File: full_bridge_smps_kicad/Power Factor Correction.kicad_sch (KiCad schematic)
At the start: 44 parts, among them Q2 MMBT2904, Q5 IPA60R280C6, Q6 IPA60R280C6, Q6 SI2309, Q7 IPW60R041C6, T1 PA1005.100NL, T2 PA1005.100NL, U4 TL431ACDBZR, U5 UCC27324D, U6 UCC27324D

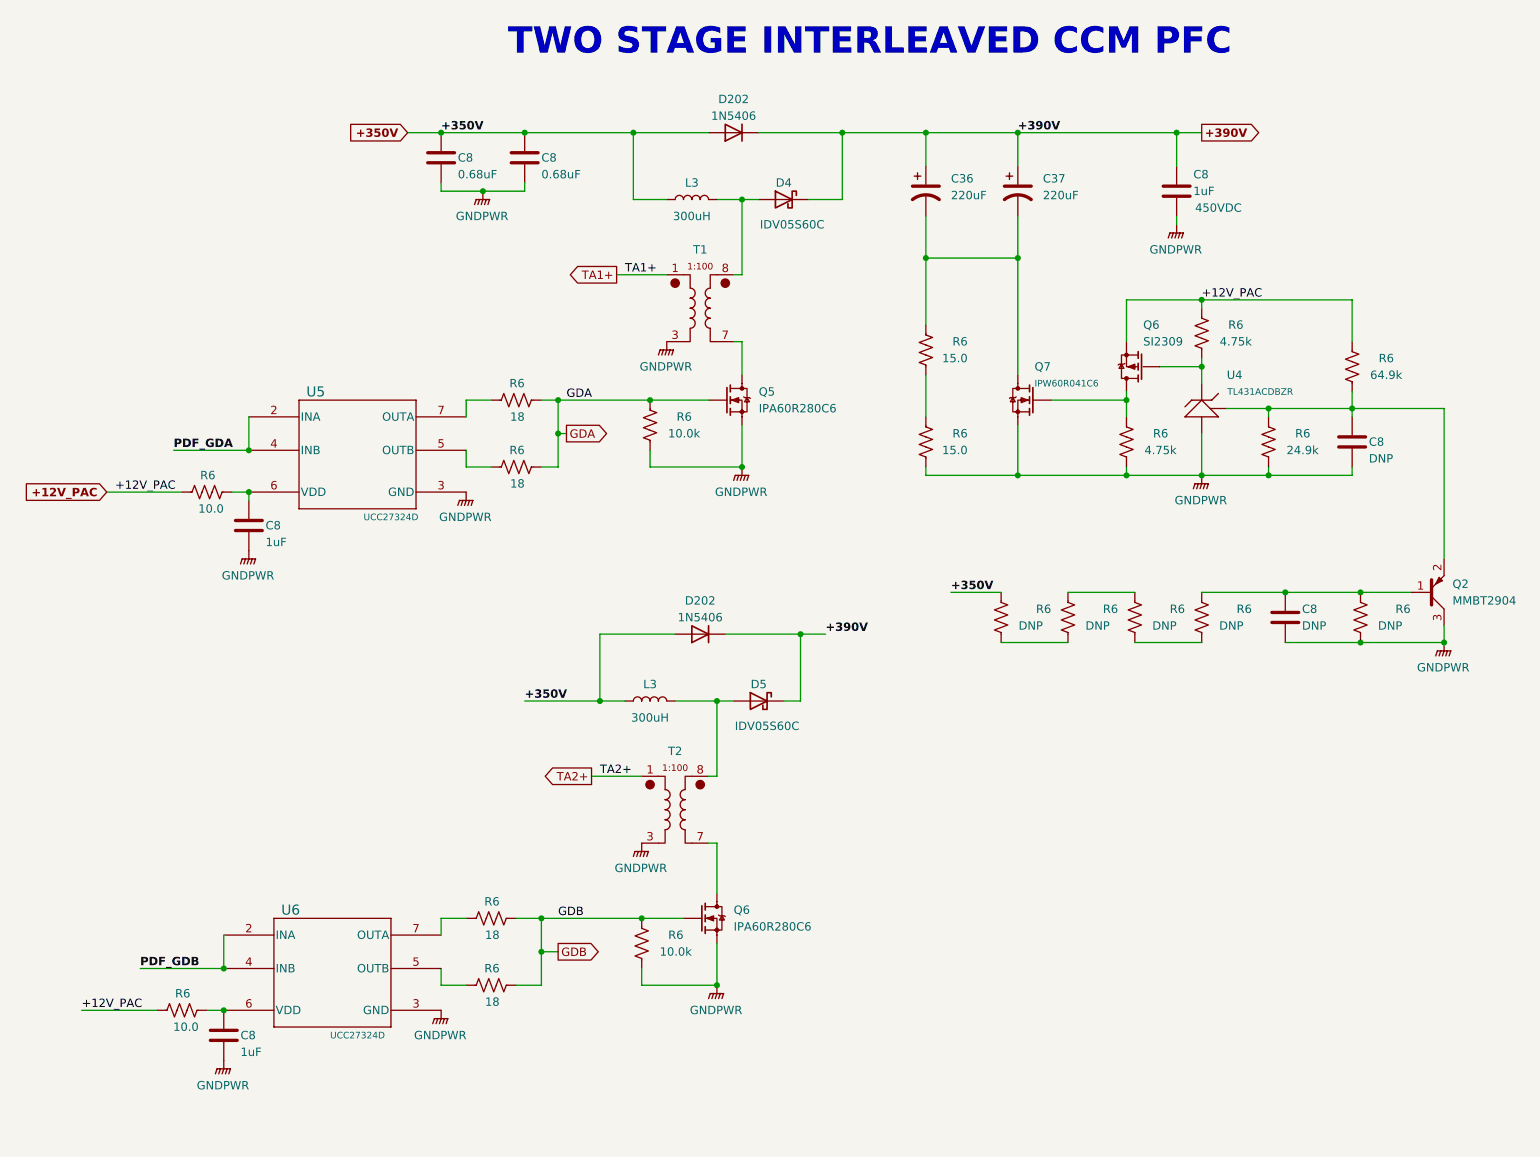
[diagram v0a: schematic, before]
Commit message: Finishing power factor correction sheets, moving to power conversion
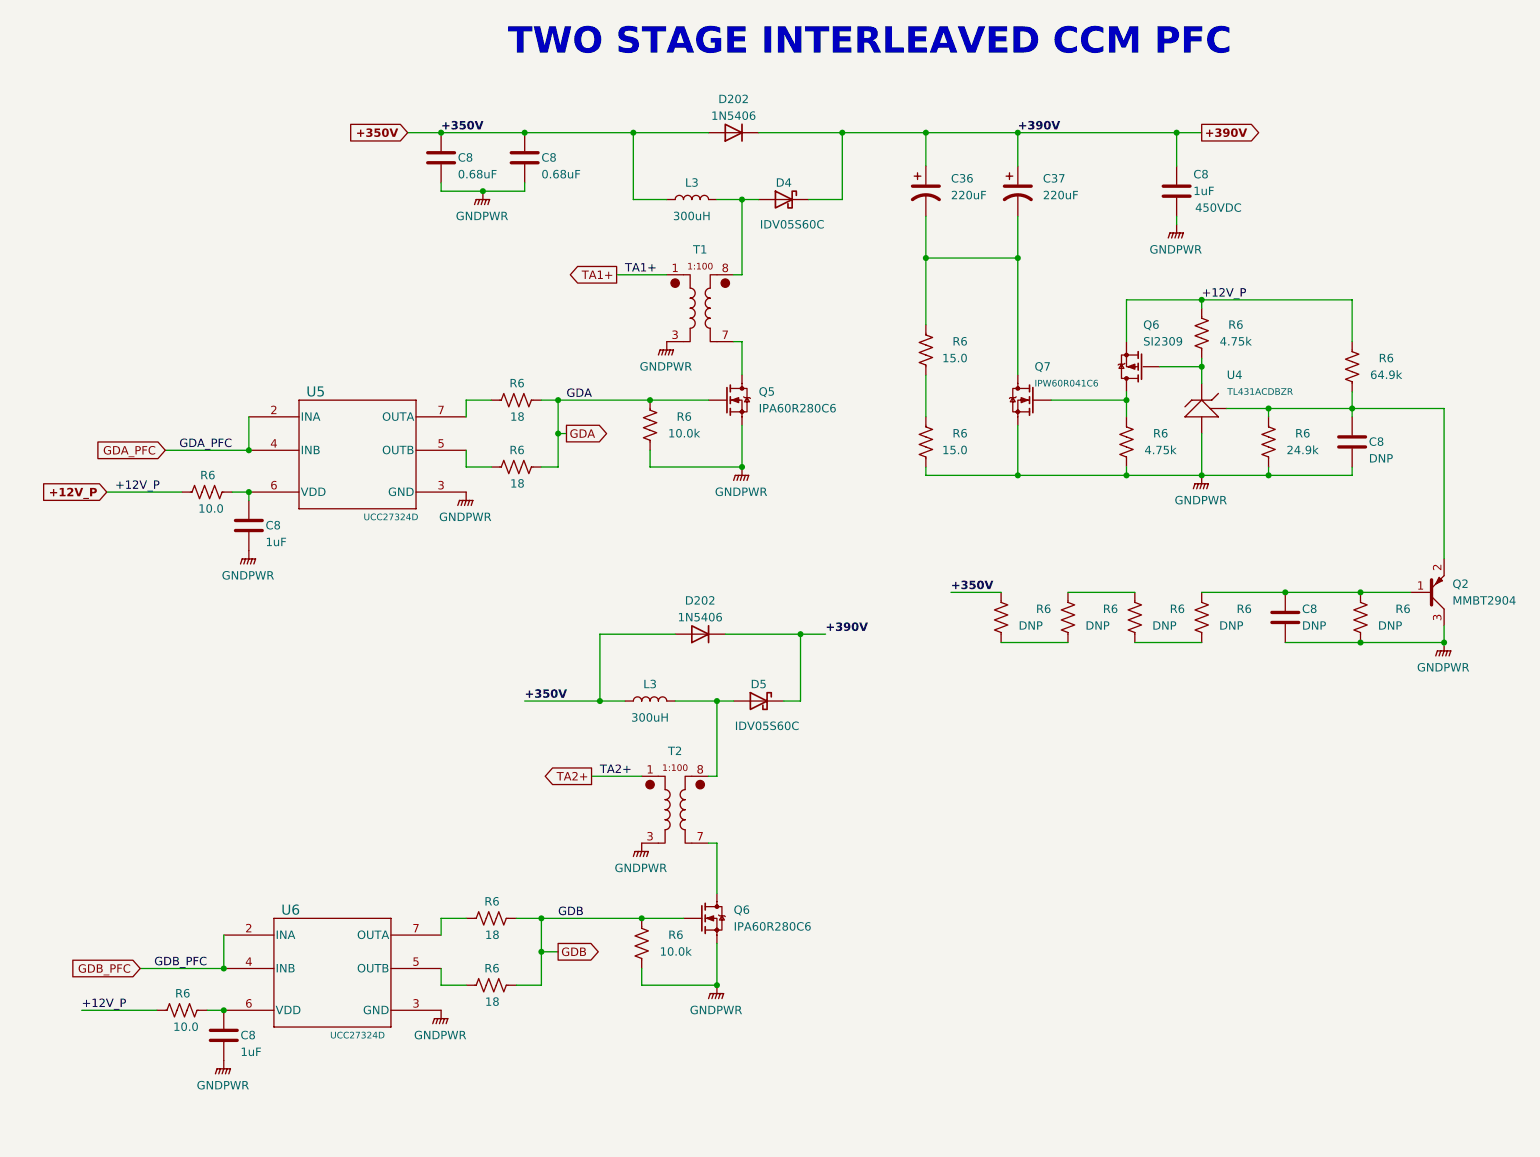
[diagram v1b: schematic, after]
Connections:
- net +12V_PAC renamed +12V_P
- net PDF_GDA renamed GDA_PFC
- net PDF_GDB renamed GDB_PFC
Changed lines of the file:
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@@
     (stroke (width 0) (type default))
   )
-  (wire (pts (xy 41.91 92.71) (xy 53.34 92.71))
+  (wire (pts (xy 40.64 92.71) (xy 53.34 92.71))
     (stroke (width 0) (type default))
   )
@@
     (effects (font (size 1.27 1.27)) (justify left bottom))
   )
-  (label "+12V_PAC" (at 27.94 177.8 0) (fields_autoplaced)
+  (label "+12V_P" (at 27.94 177.8 0) (fields_autoplaced)
     (effects (font (size 1.27 1.27)) (justify left bottom))
   )
-  (label "+12V_PAC" (at 33.02 99.06 0) (fields_autoplaced)
+  (label "+12V_P" (at 33.02 99.06 0) (fields_autoplaced)
     (effects (font (size 1.27 1.27)) (justify left bottom))
   )
@@
     (effects (font (size 1.27 1.27)) (justify left bottom))
   )
+  (label "GDA_PFC" (at 50.8 92.71 180) (fields_autoplaced)
+    (effects (font (size 1.27 1.27)) (justify right bottom))
+  )
   (label "+390V" (at 170.18 44.45 0) (fields_autoplaced)
     (effects (font (size 1.27 1.27) bold) (justify left bottom))
+  )
+  (label "GDB_PFC" (at 46.99 171.45 180) (fields_autoplaced)
+    (effects (font (size 1.27 1.27)) (justify right bottom))
   )
   (label "+350V" (at 95.25 130.81 0) (fields_autoplaced)
@@
     (effects (font (size 1.27 1.27) bold) (justify left bottom))
   )
-  (label "PDF_GDB" (at 36.83 171.45 0) (fields_autoplaced)
-    (effects (font (size 1.27 1.27) bold) (justify left bottom))
-  )
   (label "+390V" (at 140.97 120.65 0) (fields_autoplaced)
     (effects (font (size 1.27 1.27) bold) (justify left bottom))
@@
     (effects (font (size 1.27 1.27) bold) (justify left bottom))
   )
-  (label "+12V_PAC" (at 198.12 69.85 0) (fields_autoplaced)
+  (label "+12V_P" (at 198.12 69.85 0) (fields_autoplaced)
     (effects (font (size 1.27 1.27)) (justify left bottom))
   )
   (label "TA2+" (at 106.68 142.24 0) (fields_autoplaced)
     (effects (font (size 1.27 1.27)) (justify left bottom))
-  )
-  (label "PDF_GDA" (at 41.91 92.71 0) (fields_autoplaced)
-    (effects (font (size 1.27 1.27) bold) (justify left bottom))
   )
   (global_label "GDB" (shape output) (at 100.33 168.91 0) (fields_autoplaced)
@@
     )
   )
-  (global_label "+12V_PAC" (shape input) (at 31.75 99.06 180) (fields_autoplaced)
-    (effects (font (size 1.27 1.27) bold) (justify right))
-    (property "Intersheetrefs" "${INTERSHEET_REFS}" (at 18.6126 99.06 0)
+  (global_label "GDA_PFC" (shape input) (at 40.64 92.71 180) (fields_autoplaced)
+    (effects (font (size 1.27 1.27)) (justify right))
+    (property "Intersheetrefs" "${INTERSHEET_REFS}" (at 29.43 92.71 0)
       (effects (font (size 1.27 1.27)) (justify right) hide)
     )
+  )
+  (global_label "+12V_P" (shape input) (at 31.75 99.06 180) (fields_autoplaced)
+    (effects (font (size 1.27 1.27) bold) (justify right))
+    (property "Intersheetrefs" "${INTERSHEET_REFS}" (at 20.9712 99.06 0)
+      (effects (font (size 1.27 1.27)) (justify right) hide)
+    )
+  )
+  (global_label "GDB_PFC" (shape input) (at 36.83 171.45 180) (fields_autoplaced)
+    (effects (font (size 1.27 1.27)) (justify right))
+    (property "Intersheetrefs" "${INTERSHEET_REFS}" (at 25.4386 171.45 0)
+      (effects (font (size 1.27 1.27)) (justify right) hide)
+    )

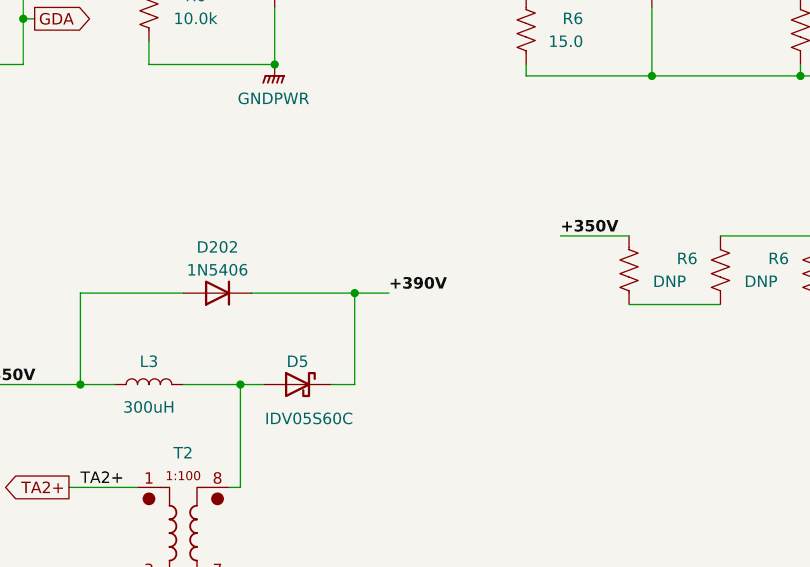
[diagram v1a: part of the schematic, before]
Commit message: Finishing up the output rectification, creating new pages for the corresponding feedback and drive circuits
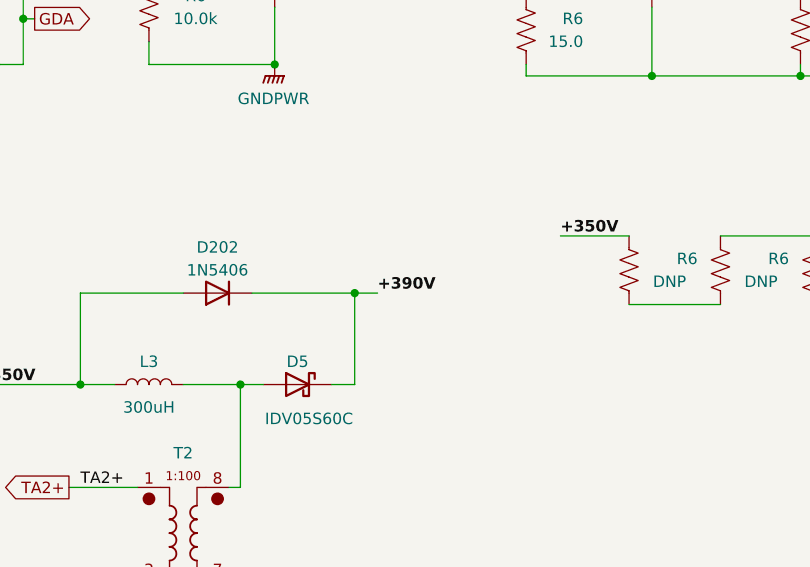
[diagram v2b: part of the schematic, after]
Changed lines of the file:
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@@
     (stroke (width 0) (type default))
   )
-  (wire (pts (xy 137.16 120.65) (xy 140.97 120.65))
+  (wire (pts (xy 137.16 120.65) (xy 139.7 120.65))
     (stroke (width 0) (type default))
   )
@@
     (effects (font (size 1.27 1.27) bold) (justify left bottom))
   )
-  (label "+390V" (at 140.97 120.65 0) (fields_autoplaced)
-    (effects (font (size 1.27 1.27) bold) (justify left bottom))
-  )
+  (label "+390V" (at 139.7 120.65 0) (fields_autoplaced)
+    (effects (font (size 1.27 1.27) bold) (justify left bottom))
+  )

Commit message: A bit of refactoring, saving work for the day
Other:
- note added: "CCM PFC A"
- note added: "CCM PFC B"
- moved on the sheet: C8, D202, D5, L3, Q6, R6, T2, U6
